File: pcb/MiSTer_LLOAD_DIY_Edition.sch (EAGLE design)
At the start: 16 parts, among them IC3 REG1117, K1 692121030100

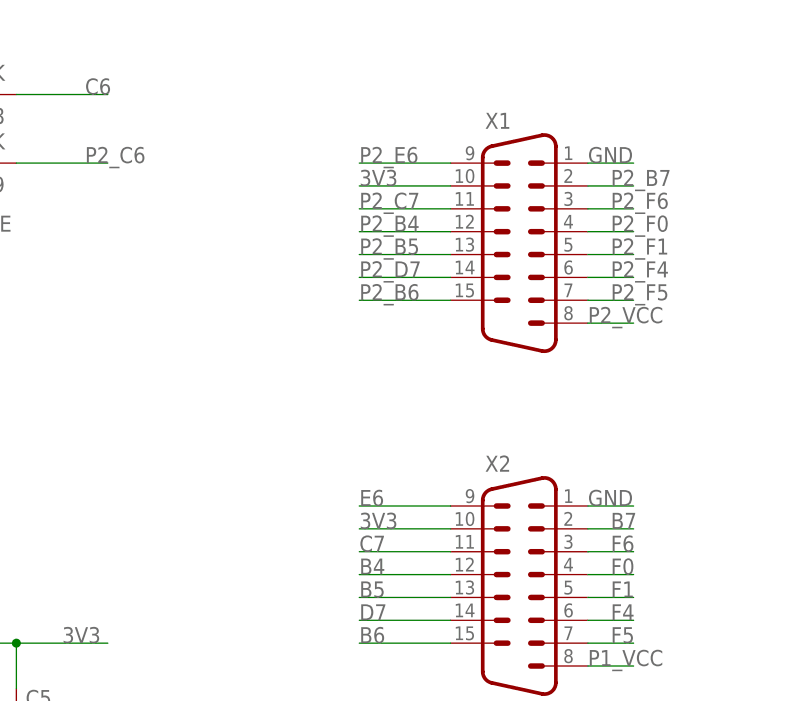
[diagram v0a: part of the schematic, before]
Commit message: Removed alternate VCC (3.3v) from DB15 pin 10. This will not make it directly compatible with supergun input, but at least no harm will be done in case someone inadvertently uses a supergun with it. Neo Geo and Neo Geo CD are still welcome in both revisions.
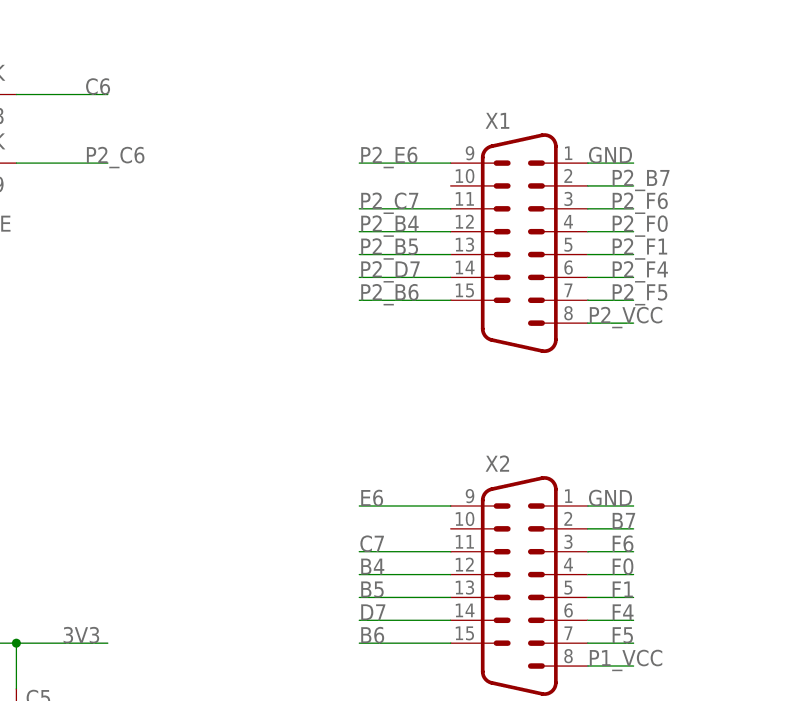
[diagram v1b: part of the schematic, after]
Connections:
- net 3V3: no longer X1.10, X2.10
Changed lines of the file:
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@@
 <label x="-7.62" y="-124.46" size="1.778" layer="95"/>
-</segment>
-<segment>
-<wire x1="35.56" y1="-73.66" x2="25.4" y2="-73.66" width="0.1524" layer="91"/>
-<label x="25.4" y="-73.66" size="1.778" layer="95"/>
-<pinref part="X1" gate="-1" pin="10"/>
-</segment>
-<segment>
-<wire x1="35.56" y1="-111.76" x2="25.4" y2="-111.76" width="0.1524" layer="91"/>
-<label x="25.4" y="-111.76" size="1.778" layer="95"/>
-<pinref part="X2" gate="-1" pin="10"/>
 </segment>
 </net>
